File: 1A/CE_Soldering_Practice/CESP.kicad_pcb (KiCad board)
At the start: 2 copper layers, 49.8 x 25.9 mm, 44 parts, among them Q1 BC847, Q2 BC847, Q3 BC847, Q4 BC847, U1 7555, U2 74HC04, U3 BA2904, U4 BA2904

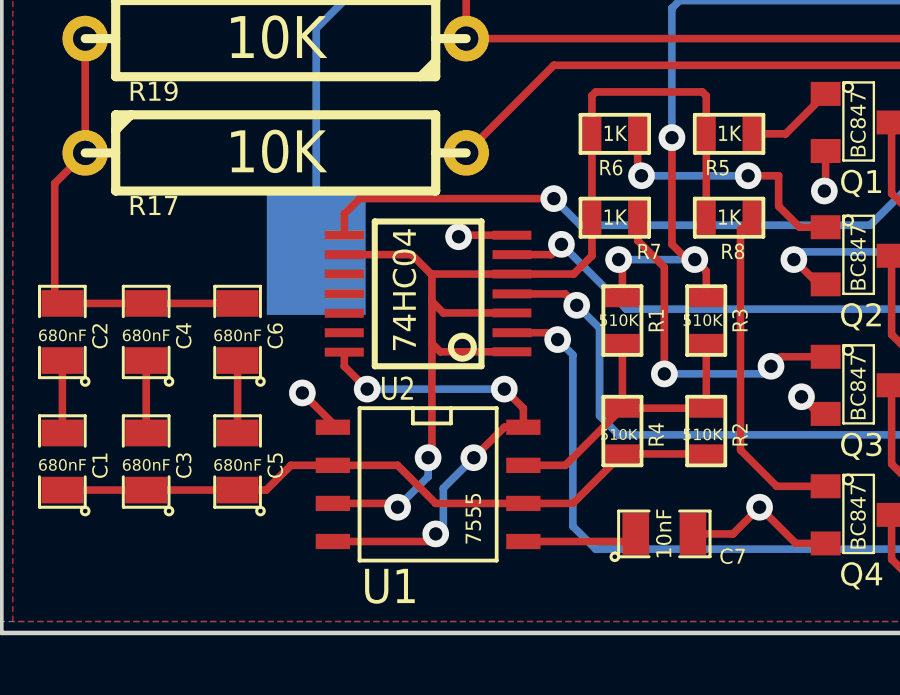
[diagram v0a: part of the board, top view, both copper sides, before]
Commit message: Remove references to unnecessary libraries; export PCB as old .brd format
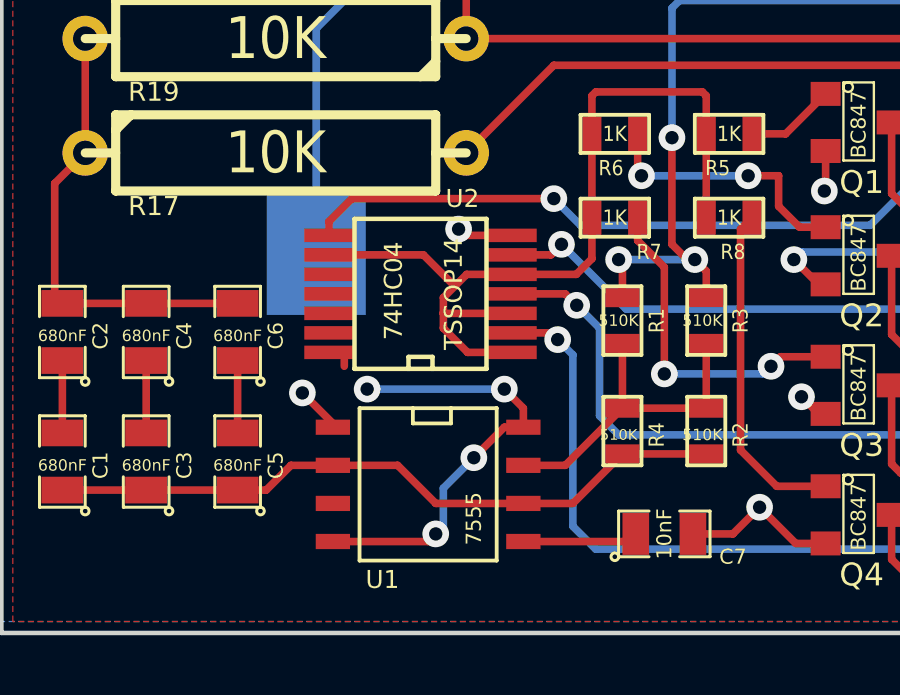
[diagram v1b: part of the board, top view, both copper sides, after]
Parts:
- U2: footprint TSSOP14 -> MM74HC04
- moved U2 0.25 mm to (170.9, 129.4)
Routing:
- net N-000003: track 38.2 -> 29.5 mm, vias 2 -> 0
- net VCC: track 58.0 -> 56.9 mm
